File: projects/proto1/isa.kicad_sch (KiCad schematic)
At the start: 35 parts, among them J2 Bus_ISA_16bit, J3 Bus_ISA_16bit, U12 PAL16L8, U13 PAL16L8

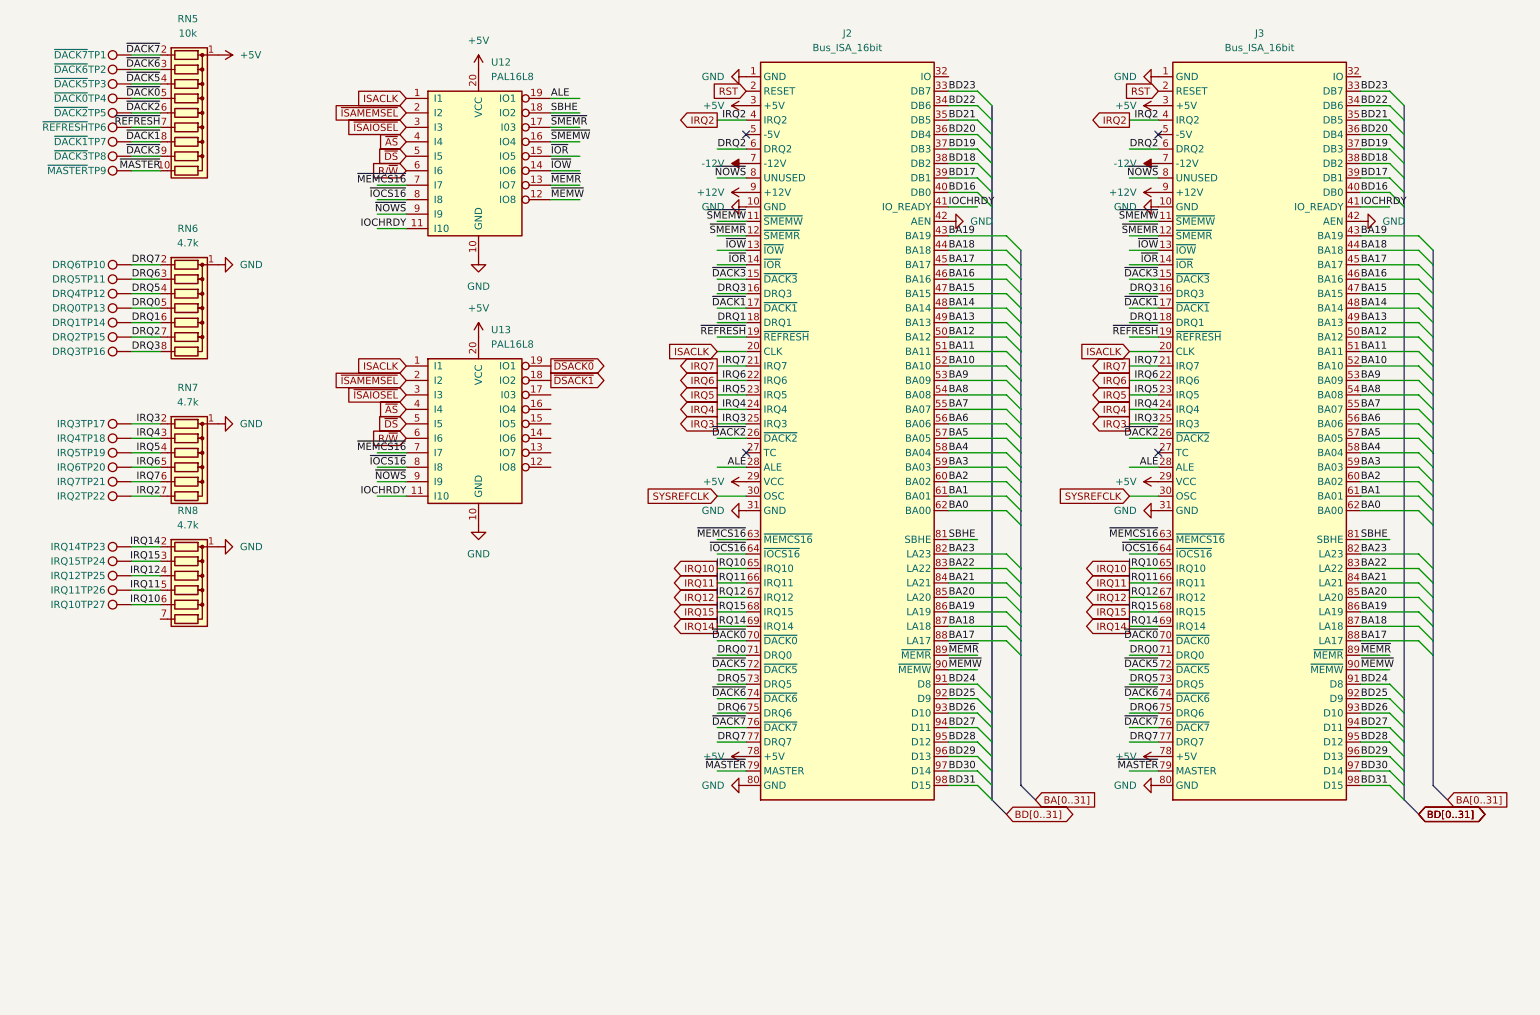
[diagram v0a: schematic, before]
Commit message: Renamed CMC to SCU, changed verification method to cocotb, and modified pcb schematic
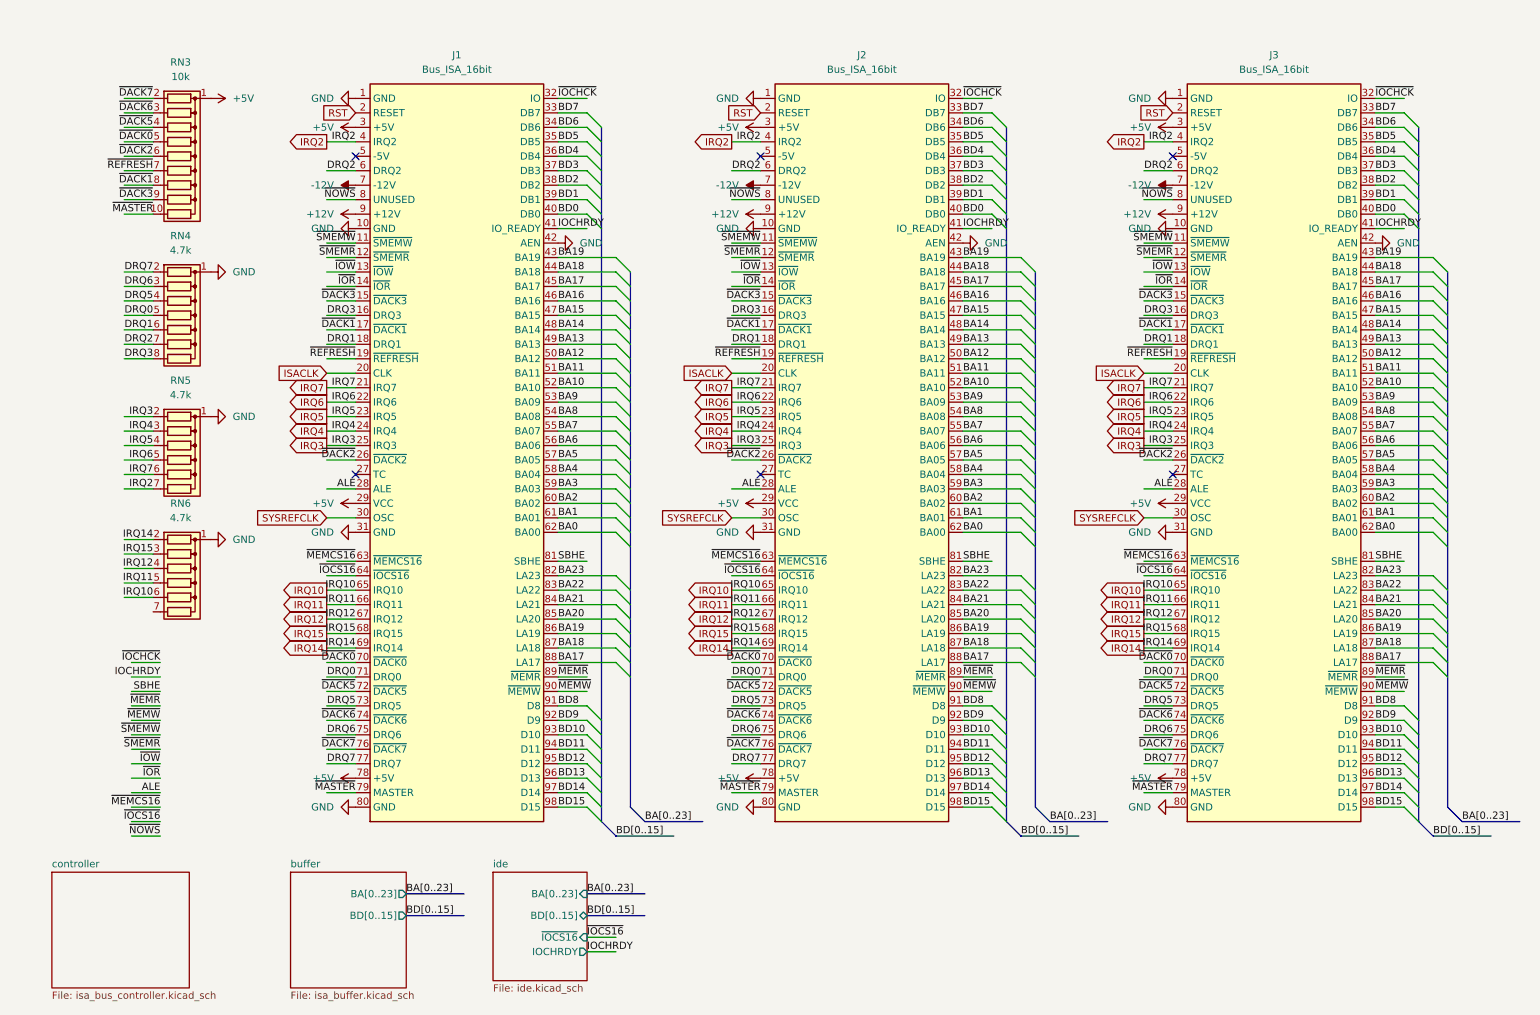
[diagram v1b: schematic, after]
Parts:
- removed TP1: ~{DACK7}, TestPoint:TestPoint_THTPad_D1.0mm_Drill0.5mm, symbol Connector:TestPoint
- removed TP10: DRQ6, TestPoint:TestPoint_THTPad_D1.0mm_Drill0.5mm, symbol Connector:TestPoint
- removed TP11: DRQ5, TestPoint:TestPoint_THTPad_D1.0mm_Drill0.5mm, symbol Connector:TestPoint
- removed TP12: DRQ4, TestPoint:TestPoint_THTPad_D1.0mm_Drill0.5mm, symbol Connector:TestPoint
- removed TP13: DRQ0, TestPoint:TestPoint_THTPad_D1.0mm_Drill0.5mm, symbol Connector:TestPoint
- removed TP14: DRQ1, TestPoint:TestPoint_THTPad_D1.0mm_Drill0.5mm, symbol Connector:TestPoint
- removed TP15: DRQ2, TestPoint:TestPoint_THTPad_D1.0mm_Drill0.5mm, symbol Connector:TestPoint
- removed TP16: DRQ3, TestPoint:TestPoint_THTPad_D1.0mm_Drill0.5mm, symbol Connector:TestPoint
- removed TP17: IRQ3, TestPoint:TestPoint_THTPad_D1.0mm_Drill0.5mm, symbol Connector:TestPoint
- removed TP18: IRQ4, TestPoint:TestPoint_THTPad_D1.0mm_Drill0.5mm, symbol Connector:TestPoint
- removed TP19: IRQ5, TestPoint:TestPoint_THTPad_D1.0mm_Drill0.5mm, symbol Connector:TestPoint
- removed TP2: ~{DACK6}, TestPoint:TestPoint_THTPad_D1.0mm_Drill0.5mm, symbol Connector:TestPoint
- removed TP20: IRQ6, TestPoint:TestPoint_THTPad_D1.0mm_Drill0.5mm, symbol Connector:TestPoint
- removed TP21: IRQ7, TestPoint:TestPoint_THTPad_D1.0mm_Drill0.5mm, symbol Connector:TestPoint
- removed TP22: IRQ2, TestPoint:TestPoint_THTPad_D1.0mm_Drill0.5mm, symbol Connector:TestPoint
- removed TP23: IRQ14, TestPoint:TestPoint_THTPad_D1.0mm_Drill0.5mm, symbol Connector:TestPoint
- removed TP24: IRQ15, TestPoint:TestPoint_THTPad_D1.0mm_Drill0.5mm, symbol Connector:TestPoint
- removed TP25: IRQ12, TestPoint:TestPoint_THTPad_D1.0mm_Drill0.5mm, symbol Connector:TestPoint
- removed TP26: IRQ11, TestPoint:TestPoint_THTPad_D1.0mm_Drill0.5mm, symbol Connector:TestPoint
- removed TP27: IRQ10, TestPoint:TestPoint_THTPad_D1.0mm_Drill0.5mm, symbol Connector:TestPoint
- removed TP3: ~{DACK5}, TestPoint:TestPoint_THTPad_D1.0mm_Drill0.5mm, symbol Connector:TestPoint
- removed TP4: ~{DACK0}, TestPoint:TestPoint_THTPad_D1.0mm_Drill0.5mm, symbol Connector:TestPoint
- removed TP5: ~{DACK2}, TestPoint:TestPoint_THTPad_D1.0mm_Drill0.5mm, symbol Connector:TestPoint
- removed TP6: ~{REFRESH}, TestPoint:TestPoint_THTPad_D1.0mm_Drill0.5mm, symbol Connector:TestPoint
- removed TP7: ~{DACK1}, TestPoint:TestPoint_THTPad_D1.0mm_Drill0.5mm, symbol Connector:TestPoint
- removed TP8: ~{DACK3}, TestPoint:TestPoint_THTPad_D1.0mm_Drill0.5mm, symbol Connector:TestPoint
- removed TP9: ~{MASTER}, TestPoint:TestPoint_THTPad_D1.0mm_Drill0.5mm, symbol Connector:TestPoint
- removed U12, U13: PAL16L8, Package_DIP:DIP-20_W7.62mm_Socket, symbol Logic_Programmable:PAL16L8
- added J1: Bus_ISA_16bit, m68k-hbc-conn:ATA_16bit, symbol Connector:Bus_ISA_16bit
- renumbered RN5 to RN3, RN6 to RN4, RN7 to RN5, RN8 to RN6
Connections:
- net +12V: now also J1.9 (+12V)
- net +5V: now also J1.29 (VCC), J1.3 (+5V), J1.78 (+5V)
- net -12V: now also J1.7 (-12V)
- net ALE: now also J1.28 (ALE)
- net BA0: now also J1.62 (BA00)
- net BA1: now also J1.61 (BA01)
- net BA10: now also J1.52 (BA10)
- net BA11: now also J1.51 (BA11)
- net BA12: now also J1.50 (BA12)
- net BA13: now also J1.49 (BA13)
- net BA14: now also J1.48 (BA14)
- net BA15: now also J1.47 (BA15)
- net BA16: now also J1.46 (BA16)
- net BA17: now also J1.45 (BA17), J1.88 (LA17)
- net BA18: now also J1.44 (BA18), J1.87 (LA18)
- net BA19: now also J1.43 (BA19), J1.86 (LA19)
- net BA2: now also J1.60 (BA02)
- net BA20: now also J1.85 (LA20)
- net BA21: now also J1.84 (LA21)
- net BA22: now also J1.83 (LA22)
- net BA23: now also J1.82 (LA23)
- net BA3: now also J1.59 (BA03)
- net BA4: now also J1.58 (BA04)
- net BA5: now also J1.57 (BA05)
- net BA6: now also J1.56 (BA06)
- net BA7: now also J1.55 (BA07)
- net BA8: now also J1.54 (BA08)
- net BA9: now also J1.53 (BA09)
- net DRQ0: now also J1.71 (DRQ0)
- net DRQ1: now also J1.18 (DRQ1)
- net DRQ2: now also J1.6 (DRQ2)
- net DRQ3: now also J1.16 (DRQ3)
- net DRQ5: now also J1.73 (DRQ5)
- net DRQ6: now also J1.75 (DRQ6)
- net DRQ7: now also J1.77 (DRQ7)
- net GND: now also J1.1 (GND), J1.10 (GND), J1.31 (GND), J1.42 (AEN), J1.80 (GND)
- net IOCHRDY: now also J1.41 (IO_READY)
- net IRQ10: now also J1.65 (IRQ10)
- net IRQ11: now also J1.66 (IRQ11)
- net IRQ12: now also J1.67 (IRQ12)
- net IRQ14: now also J1.69 (IRQ14)
- net IRQ15: now also J1.68 (IRQ15)
- net IRQ2: now also J1.4 (IRQ2)
- net IRQ3: now also J1.25 (IRQ3)
- net IRQ4: now also J1.24 (IRQ4)
- net IRQ5: now also J1.23 (IRQ5)
- net IRQ6: now also J1.22 (IRQ6)
- net IRQ7: now also J1.21 (IRQ7)
- net ISACLK: now also J1.20 (CLK)
- net RST: now also J1.2 (RESET)
- net SBHE: now also J1.81 (SBHE)
- net SYSREFCLK: now also J1.30 (OSC)
- net ~{DACK0}: now also J1.70 (~{DACK0})
- net ~{DACK1}: now also J1.17 (~{DACK1})
- net ~{DACK2}: now also J1.26 (~{DACK2})
- net ~{DACK3}: now also J1.15 (~{DACK3})
- net ~{DACK5}: now also J1.72 (~{DACK5})
- net ~{DACK6}: now also J1.74 (~{DACK6})
- net ~{DACK7}: now also J1.76 (~{DACK7})
- net ~{IOCS16}: now also J1.64 (~{IOCS16})
- net ~{IOR}: now also J1.14 (~{IOR})
- net ~{IOW}: now also J1.13 (~{IOW})
- net ~{MASTER}: now also J1.79 (MASTER)
- net ~{MEMCS16}: now also J1.63 (~{MEMCS16})
- net ~{MEMR}: now also J1.89 (~{MEMR})
- net ~{MEMW}: now also J1.90 (~{MEMW})
- net ~{NOWS}: now also J1.8 (UNUSED)
- net ~{REFRESH}: now also J1.19 (~{REFRESH})
- net ~{SMEMR}: now also J1.12 (~{SMEMR})
- net ~{SMEMW}: now also J1.11 (~{SMEMW})
- net ~{IOCHCK}: now reaches J2.32 (IO)
- net ~{IOCHCK}: now also J3.32 (IO), J1.32 (IO)
- net BD16 renamed BD0
- net BD0: now also J1.40 (DB0)
- net BD17 renamed BD1
- net BD1: now also J1.39 (DB1)
- net BD18 renamed BD2
- net BD2: now also J1.38 (DB2)
- net BD19 renamed BD3
- net BD3: now also J1.37 (DB3)
- net BD20 renamed BD4
- net BD4: now also J1.36 (DB4)
- net BD21 renamed BD5
- net BD5: now also J1.35 (DB5)
- net BD22 renamed BD6
- net BD6: now also J1.34 (DB6)
- net BD23 renamed BD7
- net BD7: now also J1.33 (DB7)
- net BD24 renamed BD8
- net BD8: now also J1.91 (D8)
- net BD25 renamed BD9
- net BD9: now also J1.92 (D9)
- net BD26 renamed BD10
- net BD10: now also J1.93 (D10)
- net BD27 renamed BD11
- net BD11: now also J1.94 (D11)
- net BD28 renamed BD12
- net BD12: now also J1.95 (D12)
- net BD29 renamed BD13
- net BD13: now also J1.96 (D13)
- net BD30 renamed BD14
- net BD14: now also J1.97 (D14)
- net BD31 renamed BD15
- net BD15: now also J1.98 (D15)
- no-connect marks 4 -> 6
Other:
- added sheet buffer (isa_buffer.kicad_sch)
- added sheet controller (isa_bus_controller.kicad_sch)
- added sheet ide (ide.kicad_sch)
- moved on the sheet: J2, J3, RN3, RN4, RN5, RN6

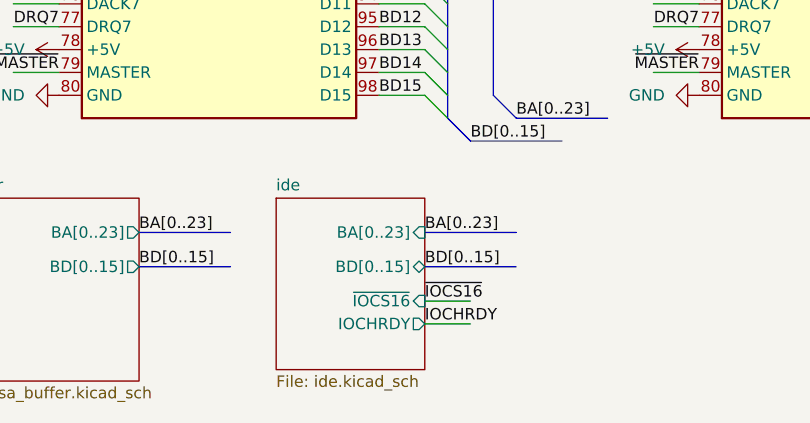
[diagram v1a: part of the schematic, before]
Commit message: Added timer and interrupt controller capability to SCU
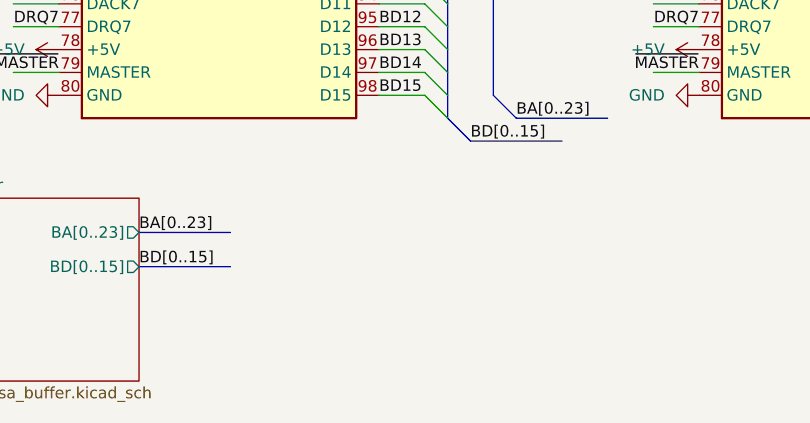
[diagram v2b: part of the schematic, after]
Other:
- removed sheet ide
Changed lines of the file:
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@@
 		)
 	)
-	(wire
-		(pts
-			(xy 121.92 180.34) (xy 116.84 180.34)
-		)
-		(stroke
-			(width 0)
-			(type default)
-		)
-	)
 	(bus
 		(pts
@@
 	(bus
 		(pts
-			(xy 116.84 173.99) (xy 127 173.99)
-		)
-		(stroke
-			(width 0)
-			(type default)
-		)
-	)
-	(bus
-		(pts
 			(xy 267.97 106.68) (xy 267.97 109.22)
 		)
@@
 	(bus
 		(pts
-			(xy 116.84 170.18) (xy 127 170.18)
-		)
-		(stroke
-			(width 0)
-			(type default)
-		)
-	)
-	(bus
-		(pts
 			(xy 267.97 129.54) (xy 267.97 132.08)
 		)
@@
 		)
 	)
-	(wire
-		(pts
-			(xy 121.92 177.8) (xy 116.84 177.8)
-		)
-		(stroke
-			(width 0)
-			(type default)
-		)
-	)
 	(bus
 		(pts
@@
 		)
 	)
-	(label "~{IOCS16}"
-		(at 116.84 177.8 0)
-		(fields_autoplaced yes)
-		(effects
-			(font
-				(size 1.27 1.27)
-			)
-			(justify left bottom)
-		)
-	)
 	(label "SBHE"
 		(at 41.91 134.62 180)
@@
 		)
 	)
-	(label "BD[0..15]"
-		(at 116.84 173.99 0)
-		(fields_autoplaced yes)
-		(effects
-			(font
-				(size 1.27 1.27)
-			)
-			(justify left bottom)
-		)
-	)
 	(label "BD2"
 		(at 182.88 45.72 0)
@@
 		)
 	)
-	(label "IOCHRDY"
-		(at 116.84 180.34 0)
-		(fields_autoplaced yes)
-		(effects
-			(font
-				(size 1.27 1.27)
-			)
-			(justify left bottom)
-		)
-	)
 	(label "BA21"
 		(at 182.88 119.38 0)
@@
 		)
 	)
-	(label "BA[0..23]"
-		(at 116.84 170.18 0)
-		(fields_autoplaced yes)
-		(effects
-			(font
-				(size 1.27 1.27)
-			)
-			(justify left bottom)
-		)
-	)
 	(global_label "IRQ12"
 		(shape output)
@@
 				)
 			)
-		)
-	)
-	(sheet
-		(at 100.33 166.37)
-		(size 16.51 19.05)
-		(fields_autoplaced yes)
-		(stroke
-			(width 0.1524)
-			(type solid)
-		)
-		(fill
-			(color 0 0 0 0.0000)
-		)
-		(property "Sheetname" "ide"
-			(at 100.33 165.6584 0)
-			(effects
-				(font
-					(size 1.27 1.27)
-				)
-				(justify left bottom)
-			)
-		)
-		(property "Sheetfile" "ide.kicad_sch"
-			(at 100.33 186.0046 0)
-			(effects
-				(font
-					(size 1.27 1.27)
-				)
-				(justify left top)
-			)
-		)
-		(pin "BD[0..15]" bidirectional
-			(at 116.84 173.99 0)
-			(effects
-				(font
-					(size 1.27 1.27)
-				)
-				(justify right)
-			)
-		)
-		(pin "BA[0..23]" input
-			(at 116.84 170.18 0)
-			(effects
-				(font
-					(size 1.27 1.27)
-				)
-				(justify right)
-			)
-		)
-		(pin "~{IOCS16}" input
-			(at 116.84 177.8 0)
-			(effects
-				(font
-					(size 1.27 1.27)
-				)
-				(justify right)
-			)
-		)
-		(pin "IOCHRDY" output
-			(at 116.84 180.34 0)
-			(effects
-				(font
-					(size 1.27 1.27)
-				)
-				(justify right)
-			)
-		)
-		(instances
-			(project "proto1"
-				(path "/e910d5a4-fa64-450e-b748-cf3a61fb2249/c4cd8f10-d1eb-4a99-9432-3d36759d5383"
-					(page "30")
-				)
-			)
